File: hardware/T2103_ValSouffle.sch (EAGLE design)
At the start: 38 parts, among them IC1 LM317MB, Q1 BSS101, T1 2N2222, U1 ATMEGA328P-PU, U2 SN74HC595N, X1 49S/18PF

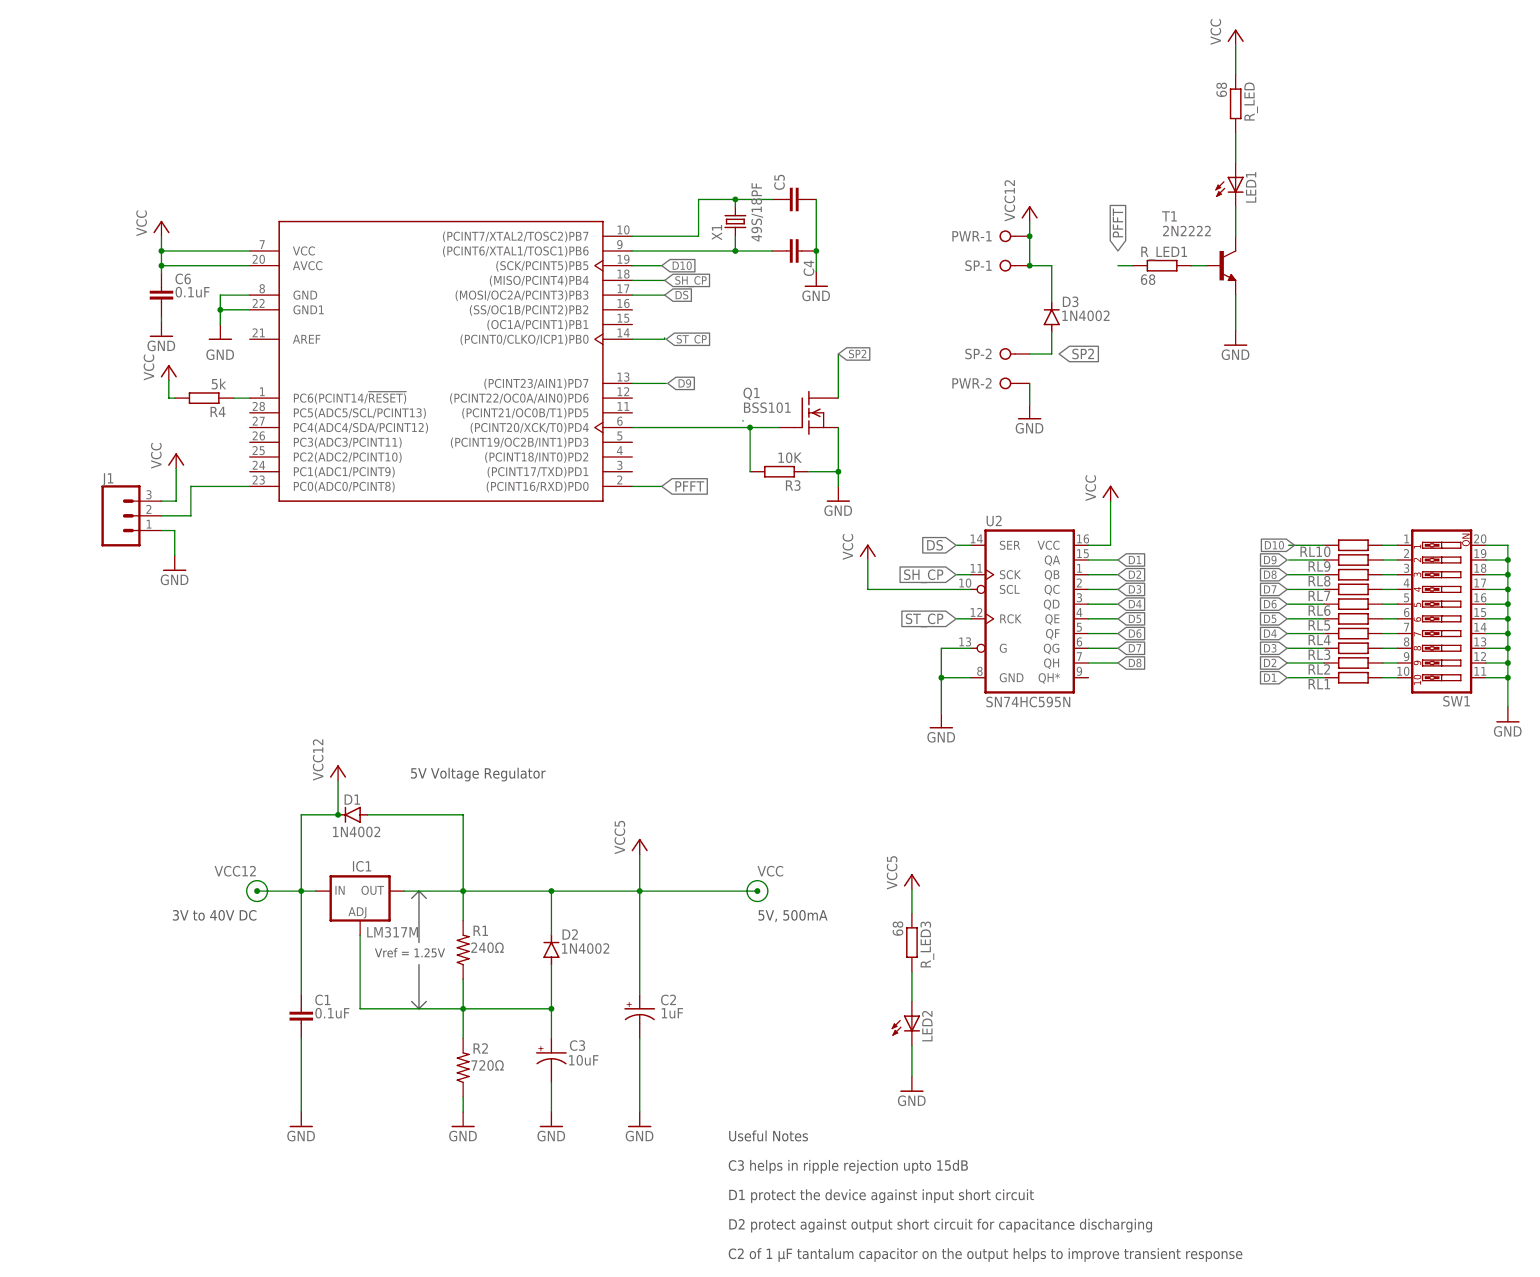
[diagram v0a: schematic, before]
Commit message: finalize routing
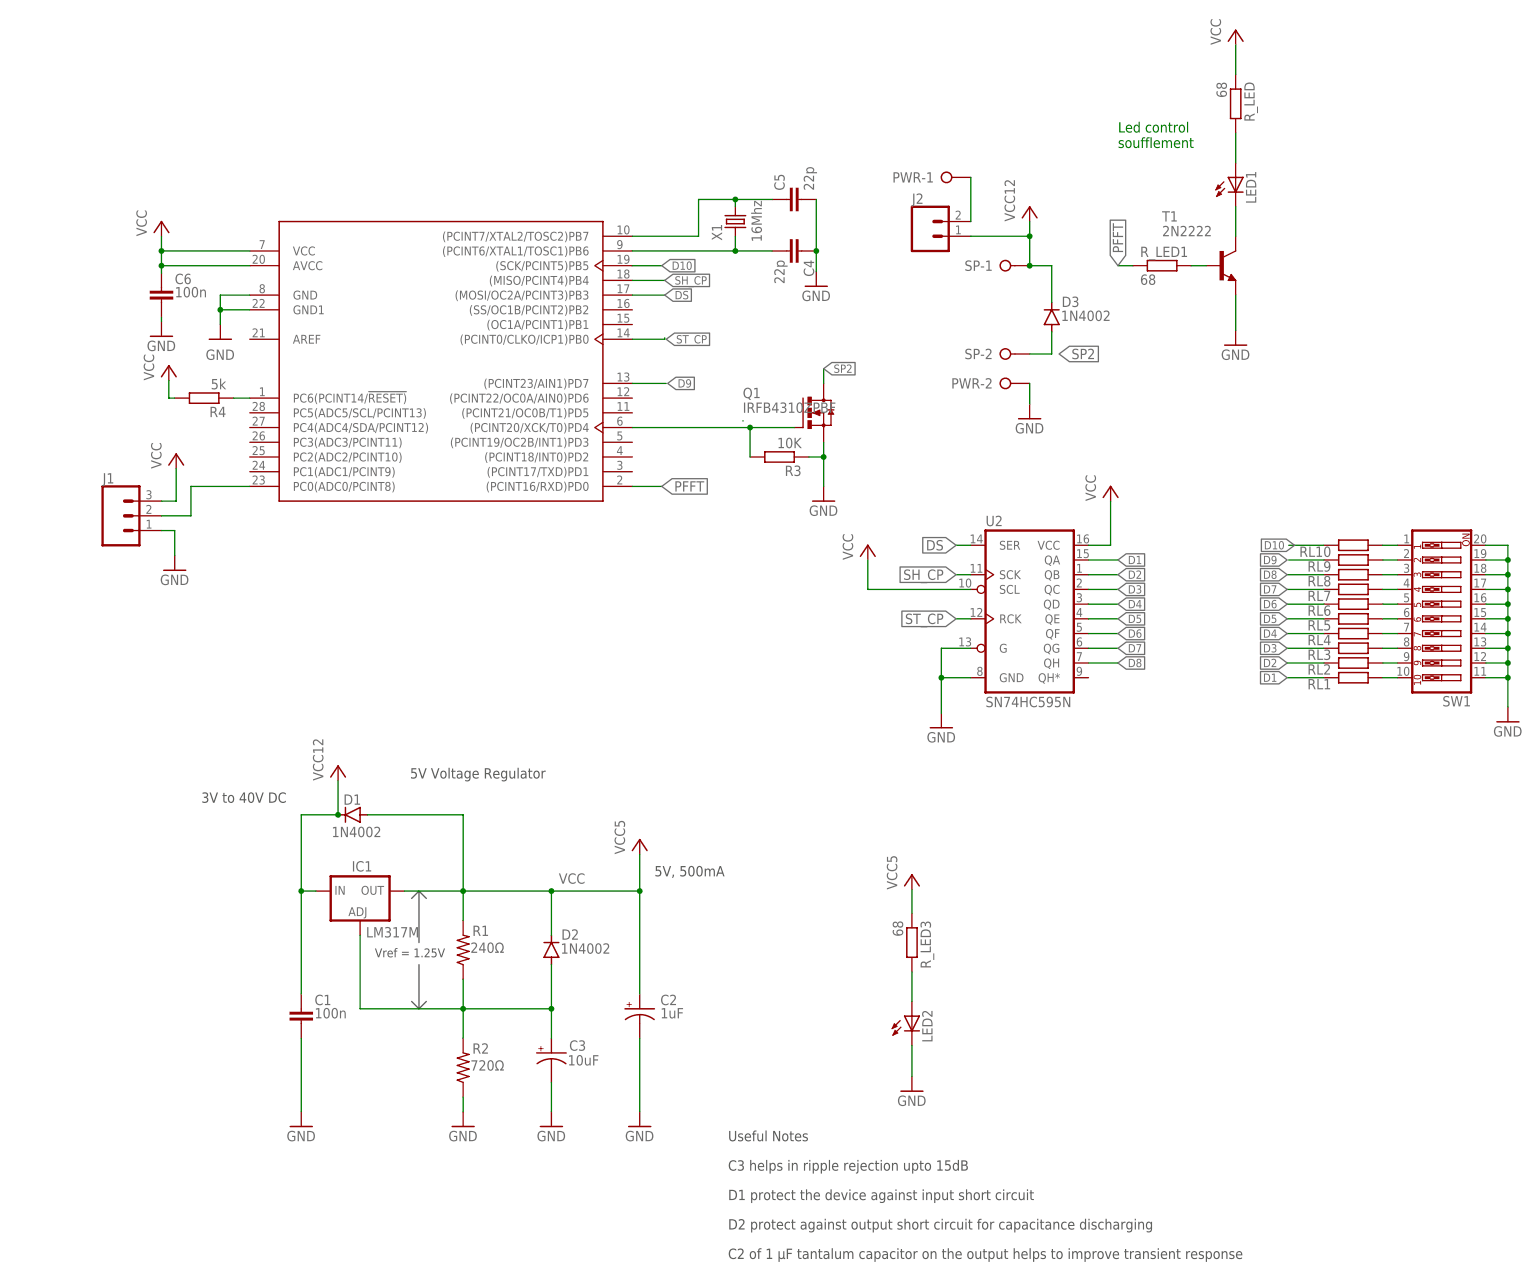
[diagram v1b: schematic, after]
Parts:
- added J2: (no value), SparkFun-Connectors:CONN_02
- C1, C6: value 0.1uF -> 100n; device rcl:C-EU075-052X106 -> rcl:C-EU050-030X075
- C2: device resistor:CPOL-USE2.5-6 -> resistor:CPOL-USE1.8-4
- C3: device resistor:CPOL-USE2-4 -> resistor:CPOL-USE1.8-4
- C4, C5: value (none) -> 22p; device resistor:C-EU025-030X050 -> resistor:C-EU025-025X050
- Q1: value BSS101 -> IRFB4310ZPBF; device transistor-fet_220:BSS101 -> Transistor:IRF520NPBF
- X1: value 49S/18PF -> 16Mhz
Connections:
- new net VCCSHUT: J2.2, PWR-1.KL
- net VCC12: now also J2.1; no longer PWR-1.KL
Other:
- note added: "Led control soufflement"
- moved on the sheet: PWR-1, R3
